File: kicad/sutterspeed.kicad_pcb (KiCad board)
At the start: 2 copper layers, 8 x 2 mm, 9 parts, among them J2 STDC10, SW2 MK-23D33-G4, U1 STM32C071G8Ux, U3 USBLC6-2P6, U4 TLV9061xDPW

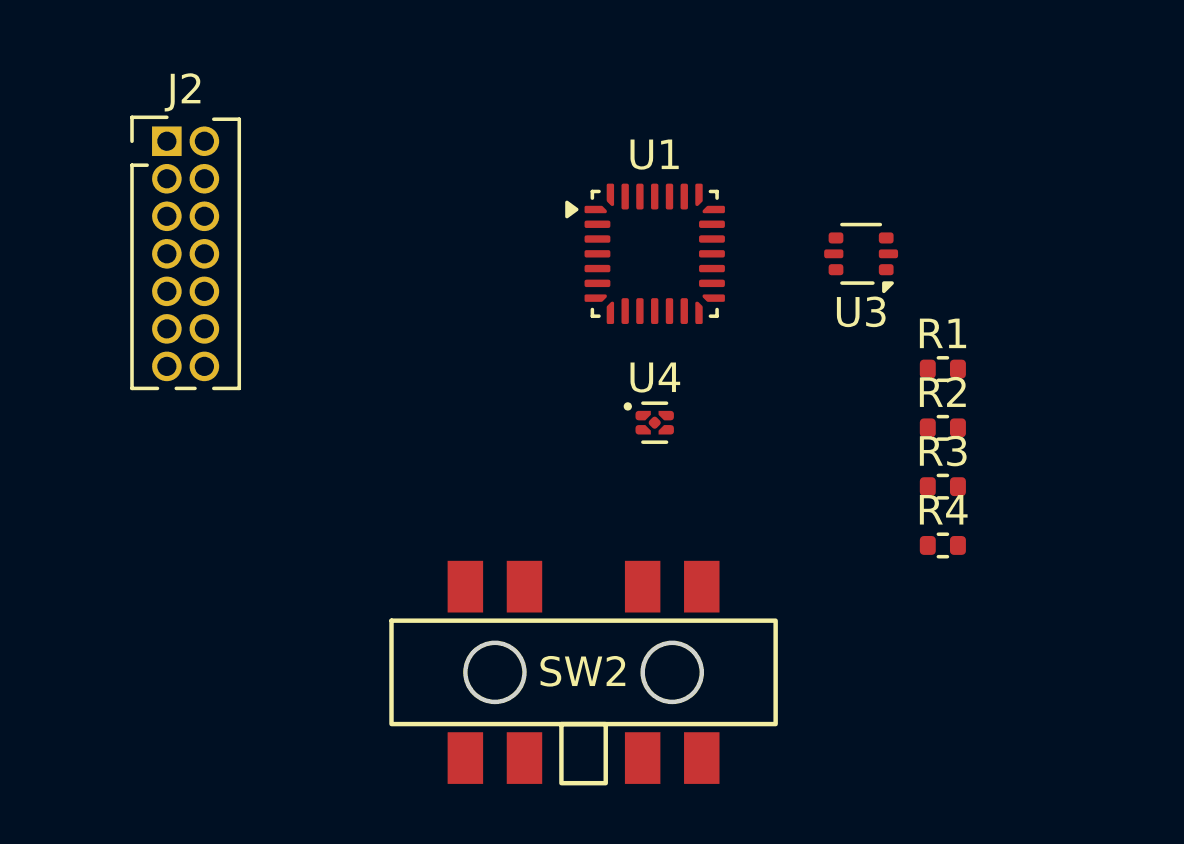
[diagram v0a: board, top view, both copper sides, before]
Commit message: Light oscilloscope firmware, Windows viewer and repository clean-up
- firmware 0.3.2: 400 kS/s scope engine (decimation, trigger, roll, shutter pulse capture), USB CDC protocol, DFU entry
- viewer (Rust/egui): scope controls, filters, measurements, cursors, shutter measurement, USB firmware update
- host test of the scope engine
- libraries as submodules; KiCad backups and local state ignored; READMEs

Co-Authored-By: Claude Opus 5.5 <noreply@anthropic.com>
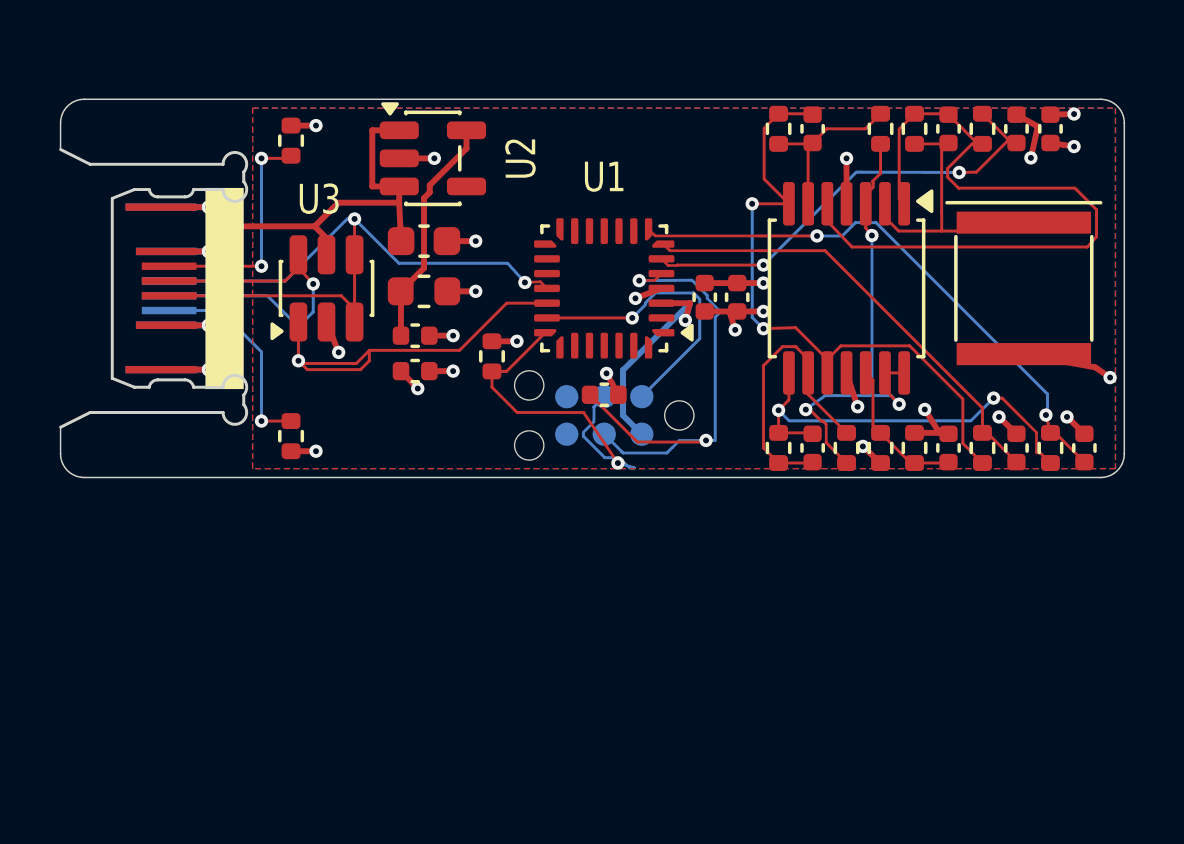
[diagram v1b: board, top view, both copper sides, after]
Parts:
- removed R4: 10k, Resistor_SMD:R_0402_1005Metric
- removed SW2: MK-23D33-G4, Sutterspeed:MK-23D33
- added C1: 10uF, Capacitor_SMD:C_0603_1608Metric, F.Cu at (112.3, 98.4)
- added C10: 100nF, Capacitor_SMD:C_0402_1005Metric, F.Cu at (133.5, 94.6)
- added C11: 1nF, Capacitor_SMD:C_0402_1005Metric, F.Cu at (132.3, 94.6)
- added C12: 1nF, Capacitor_SMD:C_0402_1005Metric, F.Cu at (132.3, 105.4)
- added C13: 10pF, Capacitor_SMD:C_0402_1005Metric, F.Cu at (125.5, 105.4)
- added C14: 1nF, Capacitor_SMD:C_0402_1005Metric, F.Cu at (134.7, 105.4)
- added C2: 1uF, Capacitor_SMD:C_0402_1005Metric, F.Cu at (112.0, 101.6)
- added C3: 1uF, Capacitor_SMD:C_0402_1005Metric, F.Cu at (112.0, 102.8)
- added C4: 100nF, Capacitor_SMD:C_0402_1005Metric, F.Cu at (121.8, 100.3)
- added C5: 1uF, Capacitor_SMD:C_0402_1005Metric, F.Cu at (122.9, 100.3)
- added C6: 100nF, Capacitor_SMD:C_0402_1005Metric, F.Cu at (118.4, 103.6)
- added C7: 47pF, Capacitor_SMD:C_0402_1005Metric, F.Cu at (130.1, 94.6)
- added C8: 10pF, Capacitor_SMD:C_0402_1005Metric, F.Cu at (125.5, 94.6)
- added C9: 100nF, Capacitor_SMD:C_0402_1005Metric, F.Cu at (130.1, 105.4)
- added D1: TEMD5510FX01, personal:Vishay_TEMD5510FX01, F.Cu at (132.6, 100.0)
- added FB1: BLM18PG221SN1D, Inductor_SMD:L_0603_1608Metric, F.Cu at (112.3, 100.1)
- added J1: PCB USB-C 14P, PCB_USBC:PCBTypeC_14P, F.Cu at (106.2, 100.0)
- added R10: 100, Resistor_SMD:R_0402_1005Metric, F.Cu at (131.2, 94.6)
- added R11: 100, Resistor_SMD:R_0402_1005Metric, F.Cu at (131.2, 105.4)
- added R12: 10k, Resistor_SMD:R_0402_1005Metric, F.Cu at (124.3, 105.4)
- added R13: 1k, Resistor_SMD:R_0402_1005Metric, F.Cu at (126.6, 105.4)
- added R14: 100, Resistor_SMD:R_0402_1005Metric, F.Cu at (133.5, 105.4)
- added R5: 10k, Resistor_SMD:R_0402_1005Metric, F.Cu at (128.9, 94.6)
- added R6: 10k, Resistor_SMD:R_0402_1005Metric, F.Cu at (124.3, 94.6)
- added R7: 1k, Resistor_SMD:R_0402_1005Metric, F.Cu at (127.8, 94.6)
- added R8: 100k, Resistor_SMD:R_0402_1005Metric, F.Cu at (127.8, 105.4)
- added R9: 10k, Resistor_SMD:R_0402_1005Metric, F.Cu at (128.9, 105.4)
- added U2: ME6211C33M5G-N, Package_TO_SOT_SMD:SOT-23-5, F.Cu at (112.6, 95.6)
- J2: value STDC10 -> SWD; footprint Connector_PinHeader_1.27mm:PinHeader_2x07_P1.27mm_Vertical -> Connector:Tag-Connect_TC2030-IDC-NL_2x03_P1.27mm_Vertical; moved to B.Cu
- R1: value 100 -> 5.1k
- R2: value 160k -> 5.1k
- R3: value 20k -> 10k
- U1: value STM32C071G8Ux -> STM32C071G8U6
- U3: value USBLC6-2P6 -> USBLC6-2SC6; footprint Package_TO_SOT_SMD:SOT-666 -> Package_TO_SOT_SMD:SOT-23-6
- U4: value TLV9061xDPW -> TLV9064IPWR; footprint Package_SON:Texas_X2SON-5_0.8x0.8mm_P0.48mm -> Package_SO:TSSOP-14_4.4x5mm_P0.65mm
- moved R1 23.4 mm to (107.8, 95.0), turned to 90 degrees
- moved R2 22.1 mm to (107.8, 105.0), turned to -90 degrees
- moved U3 18.1 mm to (109.0, 100.0), turned to 90 degrees
- moved J2 17.5 mm to (118.4, 104.3), turned to 180 degrees
- moved R3 15.9 mm to (114.6, 102.3), turned to 90 degrees
- moved U4 7.93 mm to (126.6, 100.0), turned to -90 degrees
- moved U1 2.07 mm to (118.4, 100.0), turned to 180 degrees
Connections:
- net /DEBUG_SWDIO renamed /SWDIO
- J2 pad 1: +3.3V -> +3.3VA
- J2 pad 3: GND -> /NRST
- J2 pad 4: /DEBUG_SWCLK -> /SWCLK
- R1 pad 1: GND -> /CC1
- R1 pad 2: Net-(J2-Pin_9) -> GND
- R2 pad 1: Net-(R2-Pad1) -> /CC2
- R2 pad 2: /SENSOR -> GND
- R3 pad 1: Net-(R3-Pad1) -> /SWCLK
- R3 pad 2: /SENSOR -> GND
- U1 pad 1: /RCC_OSCX_IN -> unconnected-(U1-PC14-Pad1)
- U1 pad 18: /USB_DM -> /USB_DN
- U1 pad 21: /DEBUG_SWCLK -> /SWCLK
- U1 pad 3: +3.3V -> +3.3VA
- U1 pad 6: unconnected-(U1-PA0-Pad6) -> /ADC_TIA
- U1 pad 7: unconnected-(U1-PA1-Pad7) -> /ADC_GAIN
- U1 pad 8: unconnected-(U1-PA2-Pad8) -> /ADC_GAIN2
- U3 pad 1: /USB_DM -> /USB_DP
- U3 pad 3: /USB_DP -> /USB_DN
- U3 pad 4: /USB_DP -> /USB_DN
- U3 pad 5: unconnected-(U3-VBUS-Pad5) -> VBUS
- U3 pad 6: /USB_DM -> /USB_DP
- U4 pad 1: /SENSOR -> /TIA_OUT
- U4 pad 3: +3.3V -> /VBIAS
- U4 pad 4: GND -> +3.3VA
- U4 pad 5: GND -> /TIA_OUT
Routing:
- net +3.3VA: track 0.00 -> 50.2 mm, vias 0 -> 8
- net /USB_DP: track 0.00 -> 25.0 mm, vias 0 -> 2
- net /TIA_OUT: track 0.00 -> 24.4 mm
- net GND: track 0.00 -> 23.5 mm, vias 0 -> 20
- net /USB_DN: track 0.00 -> 22.6 mm, vias 0 -> 2
- net /GAIN_OUT: track 0.00 -> 21.4 mm, vias 0 -> 2
- net /ADC_GAIN2: track 0.00 -> 19.1 mm, vias 0 -> 2
- net VBUS: track 0.00 -> 18.6 mm, vias 0 -> 2
- net /NRST: track 0.00 -> 17.3 mm, vias 0 -> 2
- net /VBIAS: track 0.00 -> 16.7 mm, vias 0 -> 3
- net /ADC_GAIN: track 0.00 -> 15.5 mm
- net /ADC_TIA: track 0.00 -> 15.2 mm, vias 0 -> 2
- net /GAIN2_OUT: track 0.00 -> 14.3 mm, vias 0 -> 2
- net /SWCLK: track 0.00 -> 12.8 mm, vias 0 -> 1
- net /SWDIO: track 0.00 -> 9.76 mm, vias 0 -> 1
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- added copper zone on B.Cu, net GND
- added copper zone on F.Cu, net GND
- added copper zone on In1.Cu, net GND
- added copper zone on In2.Cu, net GND
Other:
- board size 8 x 2 mm -> 36 x 12.8 mm
- copper layers 2 -> 4
